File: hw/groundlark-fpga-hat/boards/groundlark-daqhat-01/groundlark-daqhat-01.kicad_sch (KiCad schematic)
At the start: 0 parts

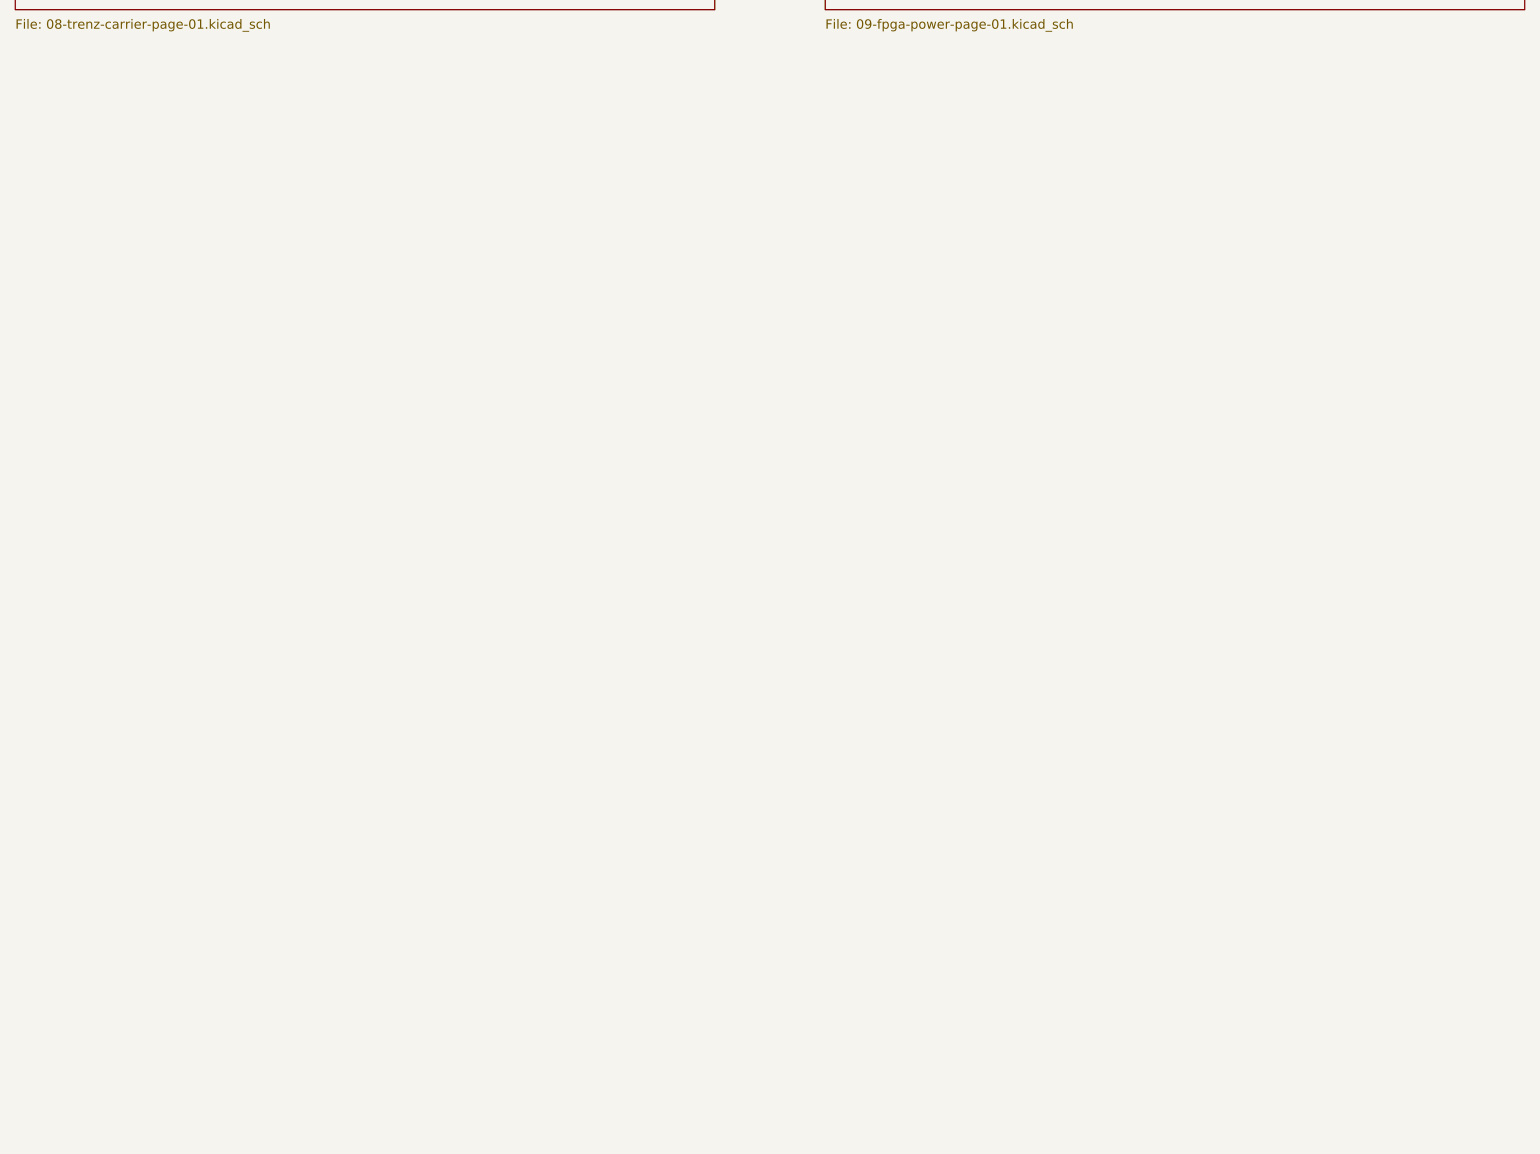
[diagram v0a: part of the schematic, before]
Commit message: Add TI Pi power supervision and expand DAQHAT enclosure
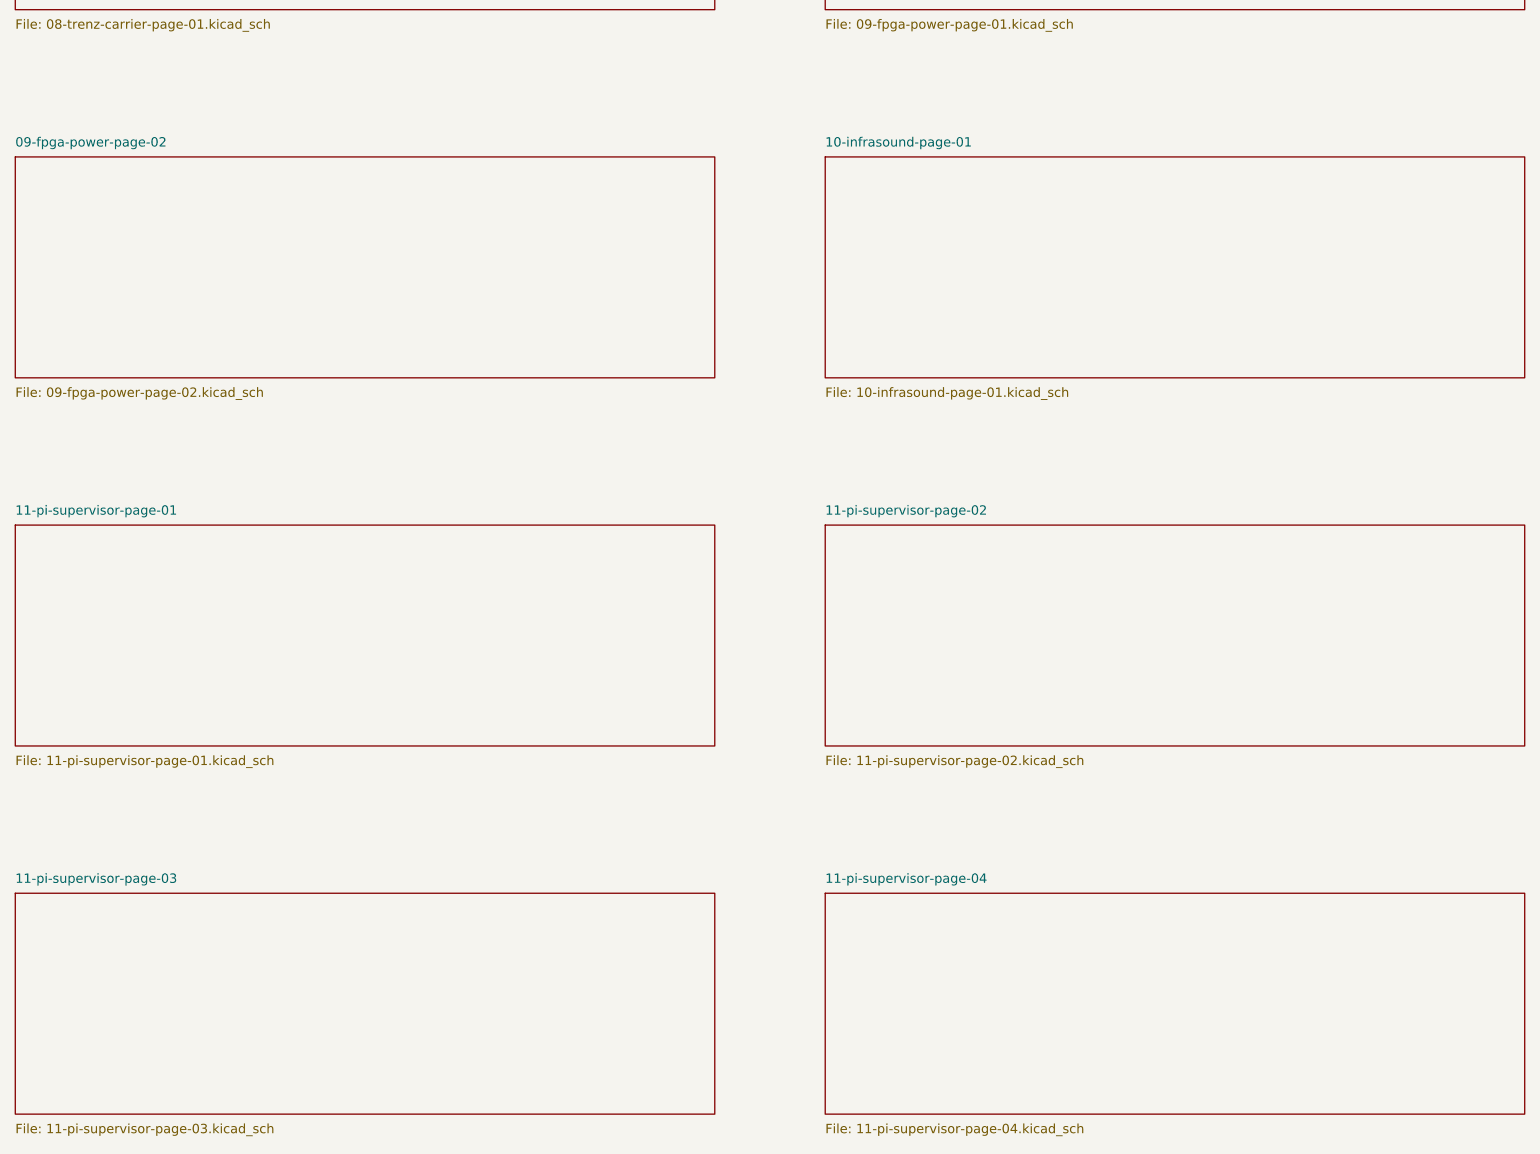
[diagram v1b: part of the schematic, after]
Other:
- added sheet 09-fpga-power-page-02 (09-fpga-power-page-02.kicad_sch)
- added sheet 10-infrasound-page-01 (10-infrasound-page-01.kicad_sch)
- added sheet 11-pi-supervisor-page-01 (11-pi-supervisor-page-01.kicad_sch)
- added sheet 11-pi-supervisor-page-02 (11-pi-supervisor-page-02.kicad_sch)
- added sheet 11-pi-supervisor-page-03 (11-pi-supervisor-page-03.kicad_sch)
- added sheet 11-pi-supervisor-page-04 (11-pi-supervisor-page-04.kicad_sch)

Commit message: Add Groundlark GNSS timing, SMA access and calibration workflow
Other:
- added sheet 04-gnss-page-01 (04-gnss-page-01.kicad_sch)

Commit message: Fix Groundlark power and GNSS electrical faults
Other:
- added sheet 04-gnss-page-02 (04-gnss-page-02.kicad_sch)

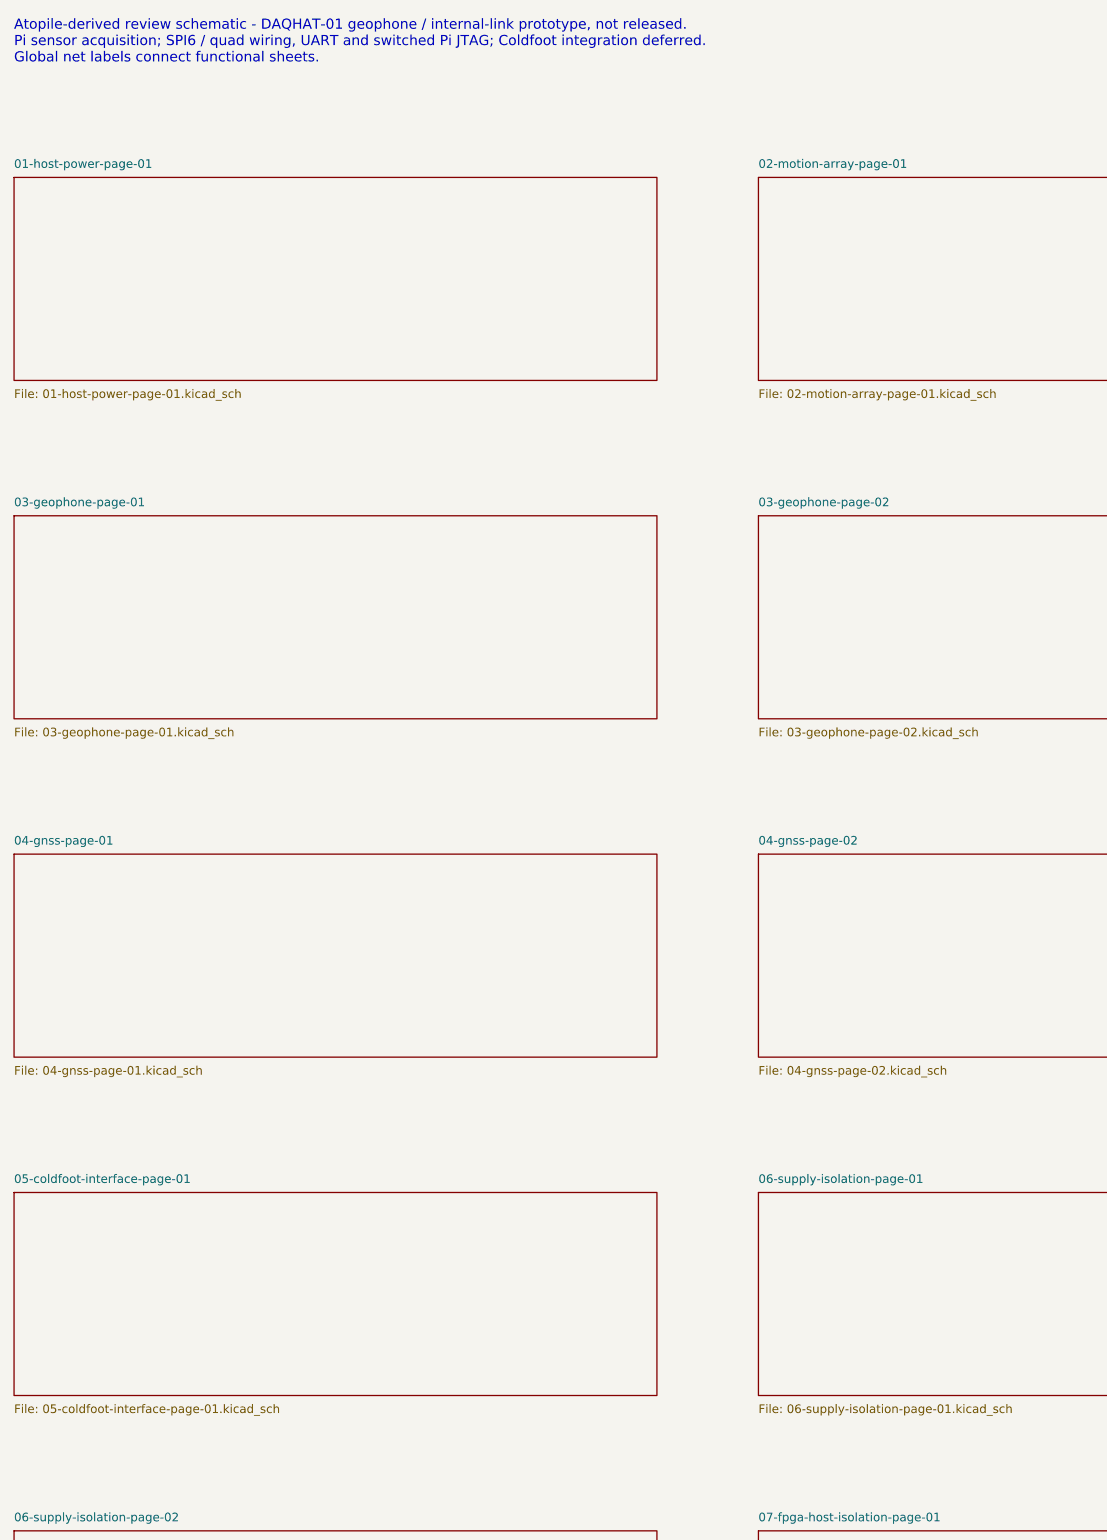
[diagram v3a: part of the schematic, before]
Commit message: Remove retired ASIC HAT variant and references
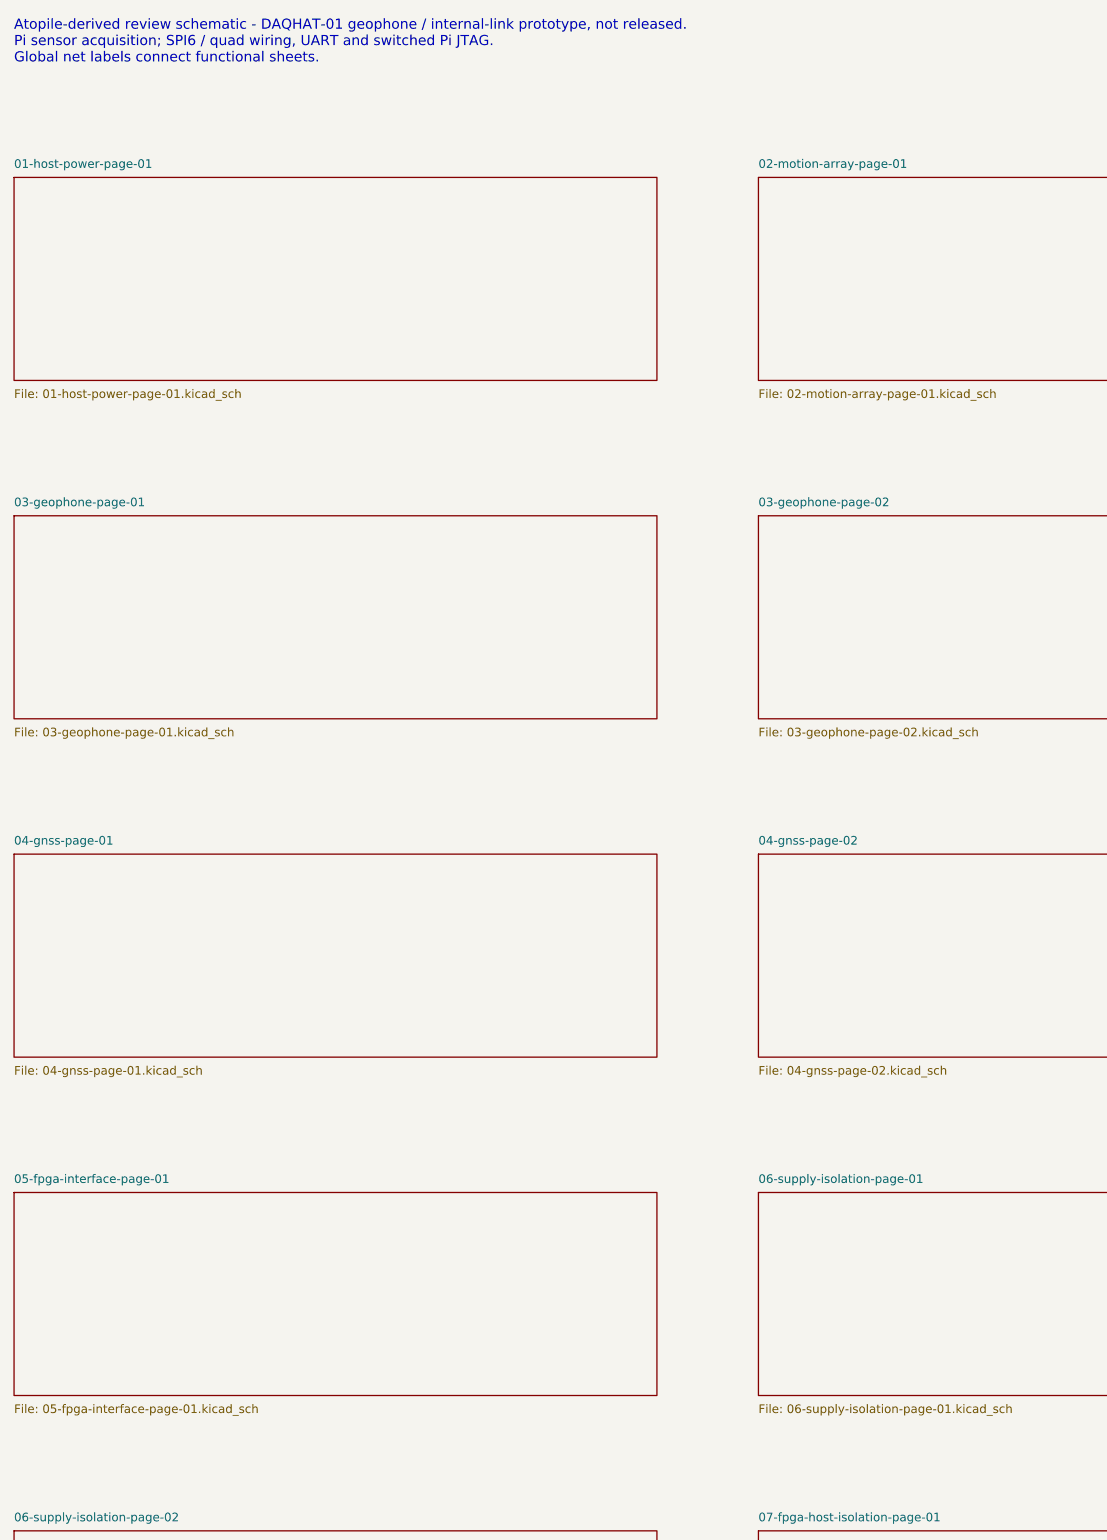
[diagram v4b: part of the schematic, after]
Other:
- sheet 05-coldfoot-interface-page-01 renamed 05-fpga-interface-page-01
- sheet 05-fpga-interface-page-01: file 05-coldfoot-interface-page-01.kicad_sch -> 05-fpga-interface-page-01.kicad_sch
- note added: "Atopile-derived review schematic - DAQHAT-01 geophone / internal-link prototype, not released. Pi sensor acquisition; SPI6 / quad wiring, UART and switched Pi JTAG. Global net labels connect functional sheets."
- note removed: "Atopile-derived review schematic - DAQHAT-01 geophone / internal-link prototype, not released. Pi sensor acquisition; SPI6 / quad wiring, UART and switched Pi JTAG; Coldfoot integration deferred. Global net labels connect functional sheets."
